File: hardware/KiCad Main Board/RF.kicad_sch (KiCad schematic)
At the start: 29 parts, among them U4 SI4468-A2A-IM, U6 CC1120RHBR, Y2 RTX-104EF3C-S-30.000-TR, Y3 END4263D-32M

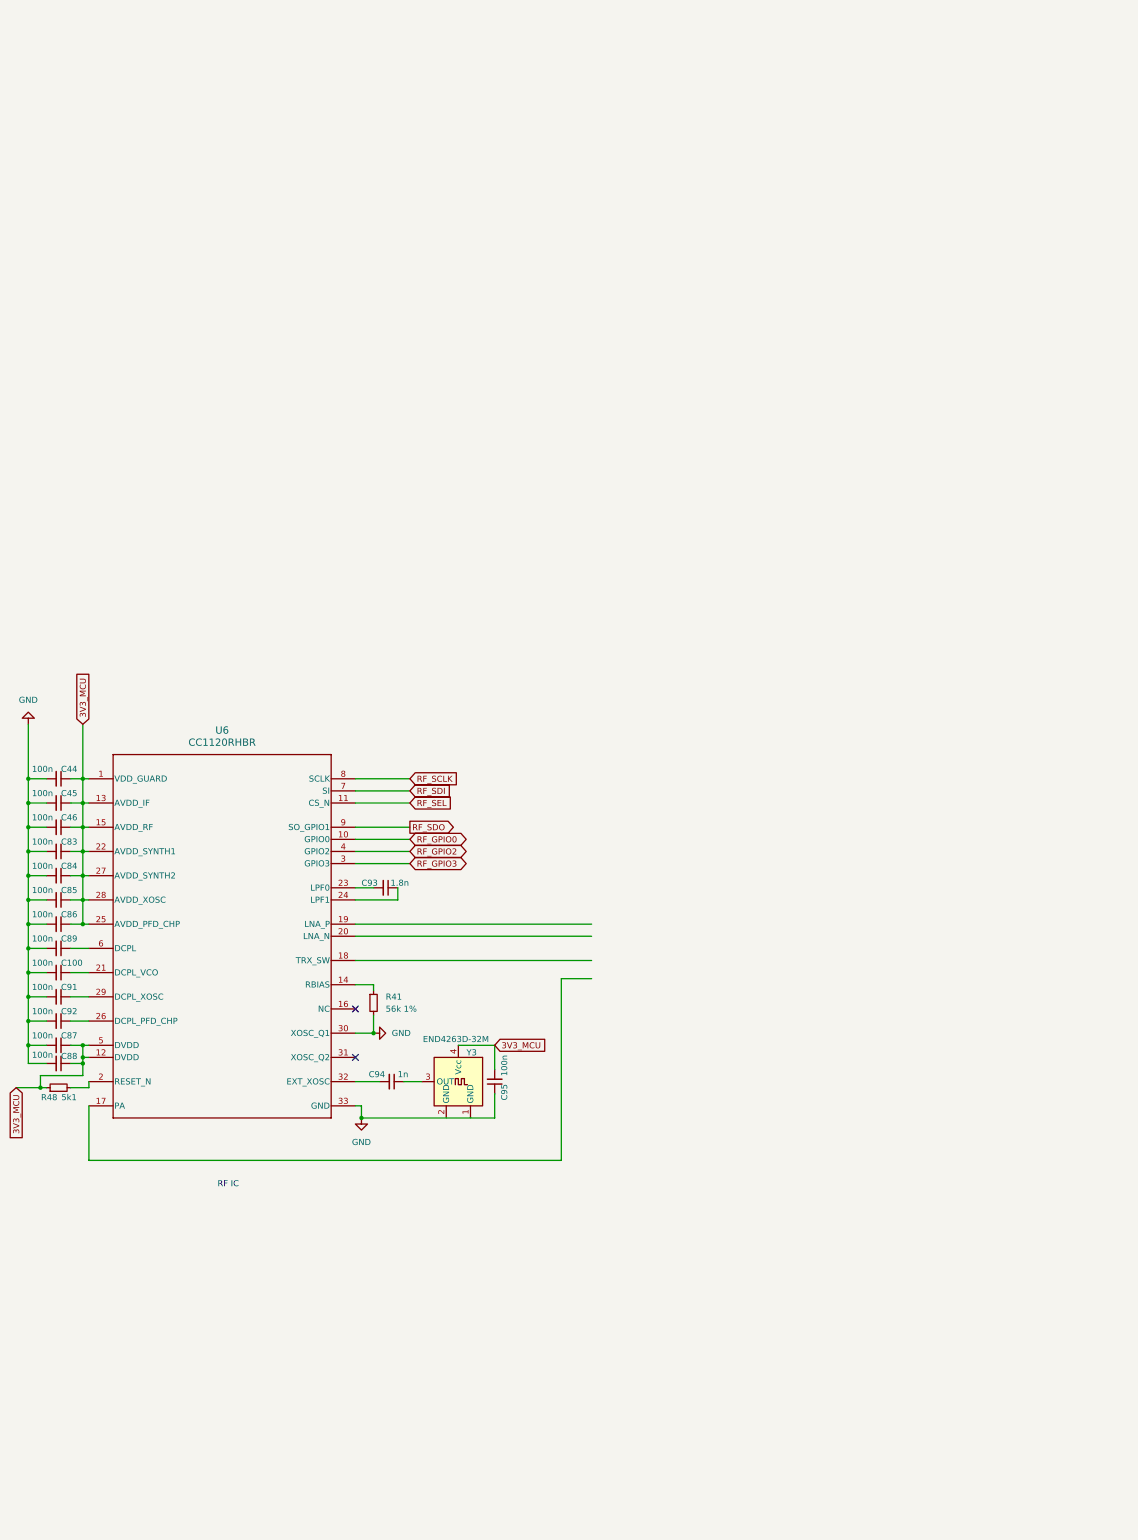
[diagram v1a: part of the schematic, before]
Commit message: added connector for RF daughter board
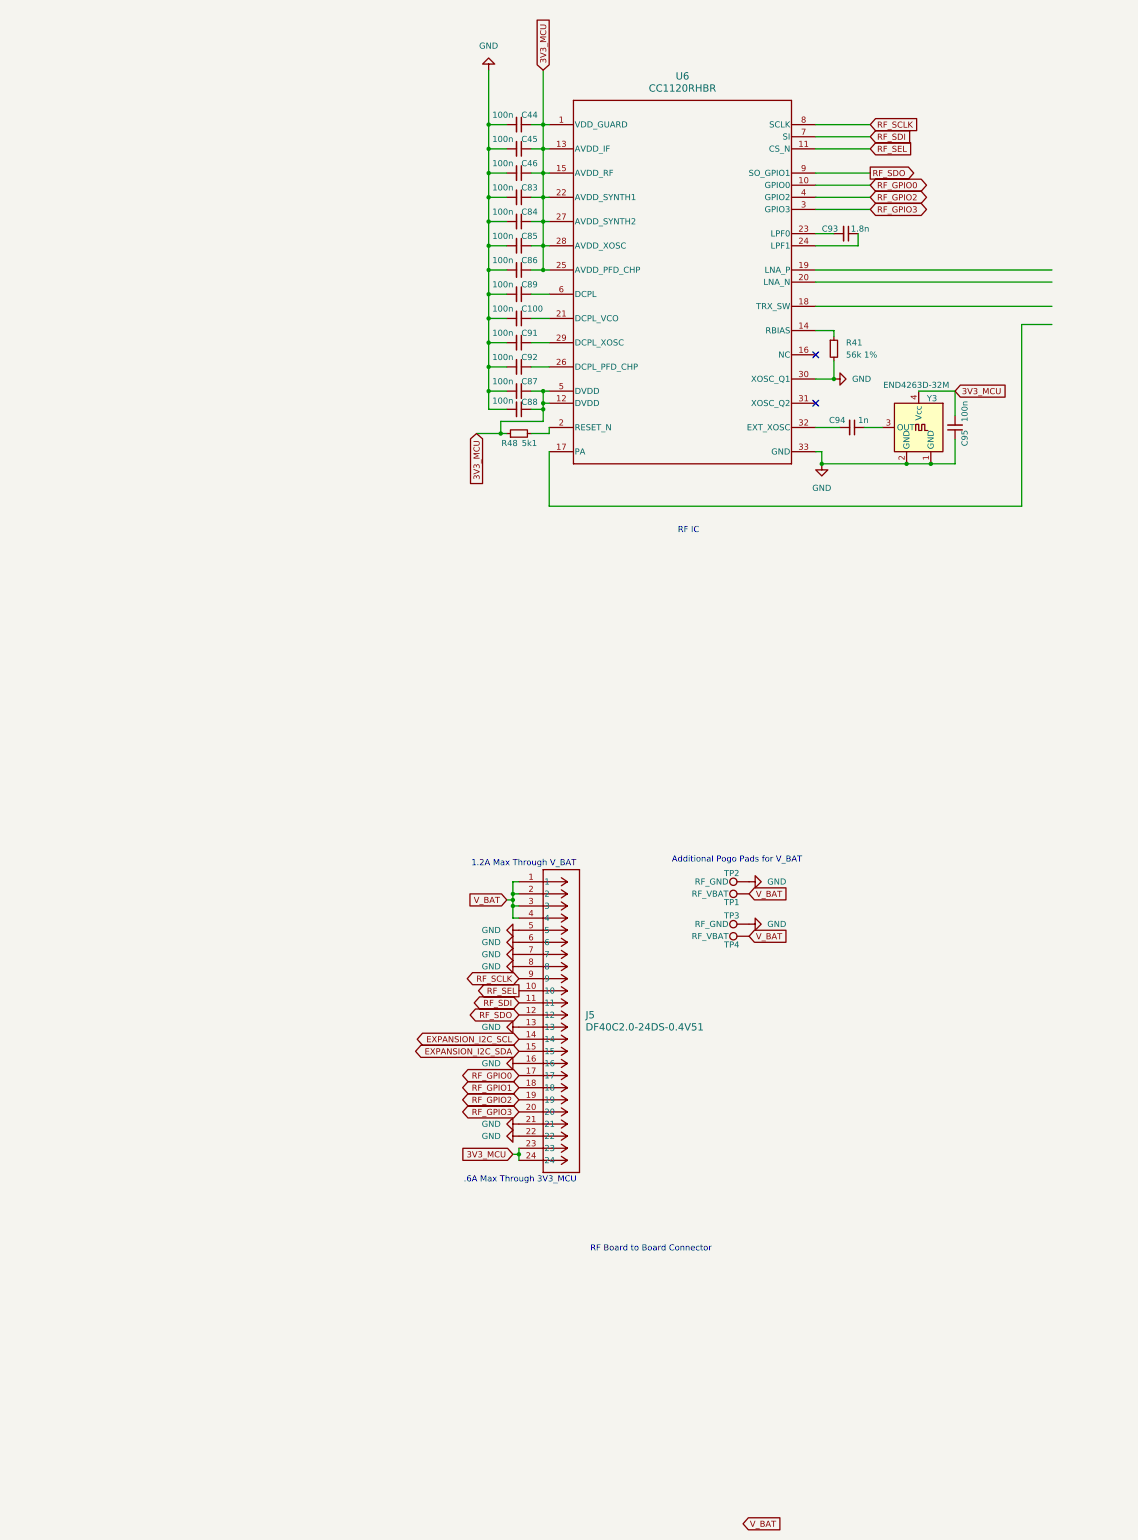
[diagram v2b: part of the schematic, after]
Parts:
- added J5: DF40C2.0-24DS-0.4V51, CONN24_DF40C-2-24DS_HIR, symbol 2025-04-19_21-20-12:DF40C2.0-24DS-0.4V51
- added TP1, TP4: RF_VBAT, TestPoint:TestPoint_Pad_D2.5mm, symbol Connector:TestPoint
- added TP2, TP3: RF_GND, TestPoint:TestPoint_Pad_D2.5mm, symbol Connector:TestPoint
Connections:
- net 3V3_MCU: now also J5.23, J5.24
- net GND: now also Y3.1 (GND), Y3.2 (GND), J5.13, J5.16, J5.21, J5.22, J5.5, J5.6, J5.7, J5.8, TP2.1, TP3.1
- net RF_GPIO0: now also J5.17
- net RF_GPIO1: now also J5.18
- net RF_GPIO2: now also J5.19
- net RF_GPIO3: now also J5.20
- net RF_SCLK: now also J5.9
- net RF_SDI: now also J5.11
- net RF_SDO: now also J5.12
- net RF_SEL: now also J5.10
- new net EXPANSION_I2C_SCL: J5.14
- new net EXPANSION_I2C_SDA: J5.15
- new net V_BAT: J5.1, J5.2, J5.3, J5.4, TP1.1, TP4.1
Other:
- note added: ".6A Max Through 3V3_MCU"
- note added: "1.2A Max Through V_BAT"
- note added: "Additional Pogo Pads for V_BAT"
- note added: "RF Board to Board Connector"
- moved on the sheet: C100, C44, C45, C46, C83, C84, C85, C86, C87, C88, C89, C91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

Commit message: working on PCB
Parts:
- removed C20: 4.7u, symbol Device:C_Small
- removed C21, C24: 100n, symbol Device:C_Small
- removed C22, C25: 100p, symbol Device:C_Small
- removed C23: 15p, symbol Device:C_Small
- removed R11: 10k, symbol Device:R_Small
- removed U4: SI4468-A2A-IM, QFN20_4X4_SIL, symbol 2025-03-28_00-57-05:SI4468-A2A-IM
- removed Y2: RTX-104EF3C-S-30.000-TR, Crystal:Crystal_SMD_3225-4Pin_3.2x2.5mm, symbol Device:Crystal_GND23
- added U14: AT24CS01-SSHM, Package_SO:SOIC-8_3.9x4.9mm_P1.27mm, symbol Memory_EEPROM:AT24CS01-SSHM
- J5: footprint CONN24_DF40C-2-24DS_HIR -> DF40C-24DS:CONN24_DF40C-2-24DS_HIR
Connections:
- net EXPANSION_I2C_SDA: now also J5.13; no longer J5.15
- net GND: now also J5.10, J5.11, J5.12, J5.9; no longer J5.13, J5.16, J5.21, J5.22, J5.5
- net RF_GPIO0: now also J5.19; no longer J5.17
- net RF_GPIO1: now also J5.20; no longer J5.18
- net RF_GPIO2: now also J5.21; no longer J5.19
- net RF_GPIO3: now also J5.22; no longer J5.20
- net RF_SCLK: now also J5.15; no longer J5.9
- net RF_SDI: now also J5.16; no longer J5.11
- net RF_SDO: now also J5.17; no longer J5.12
- net RF_SEL: now also J5.18; no longer J5.10
- net V_BAT: now also J5.5

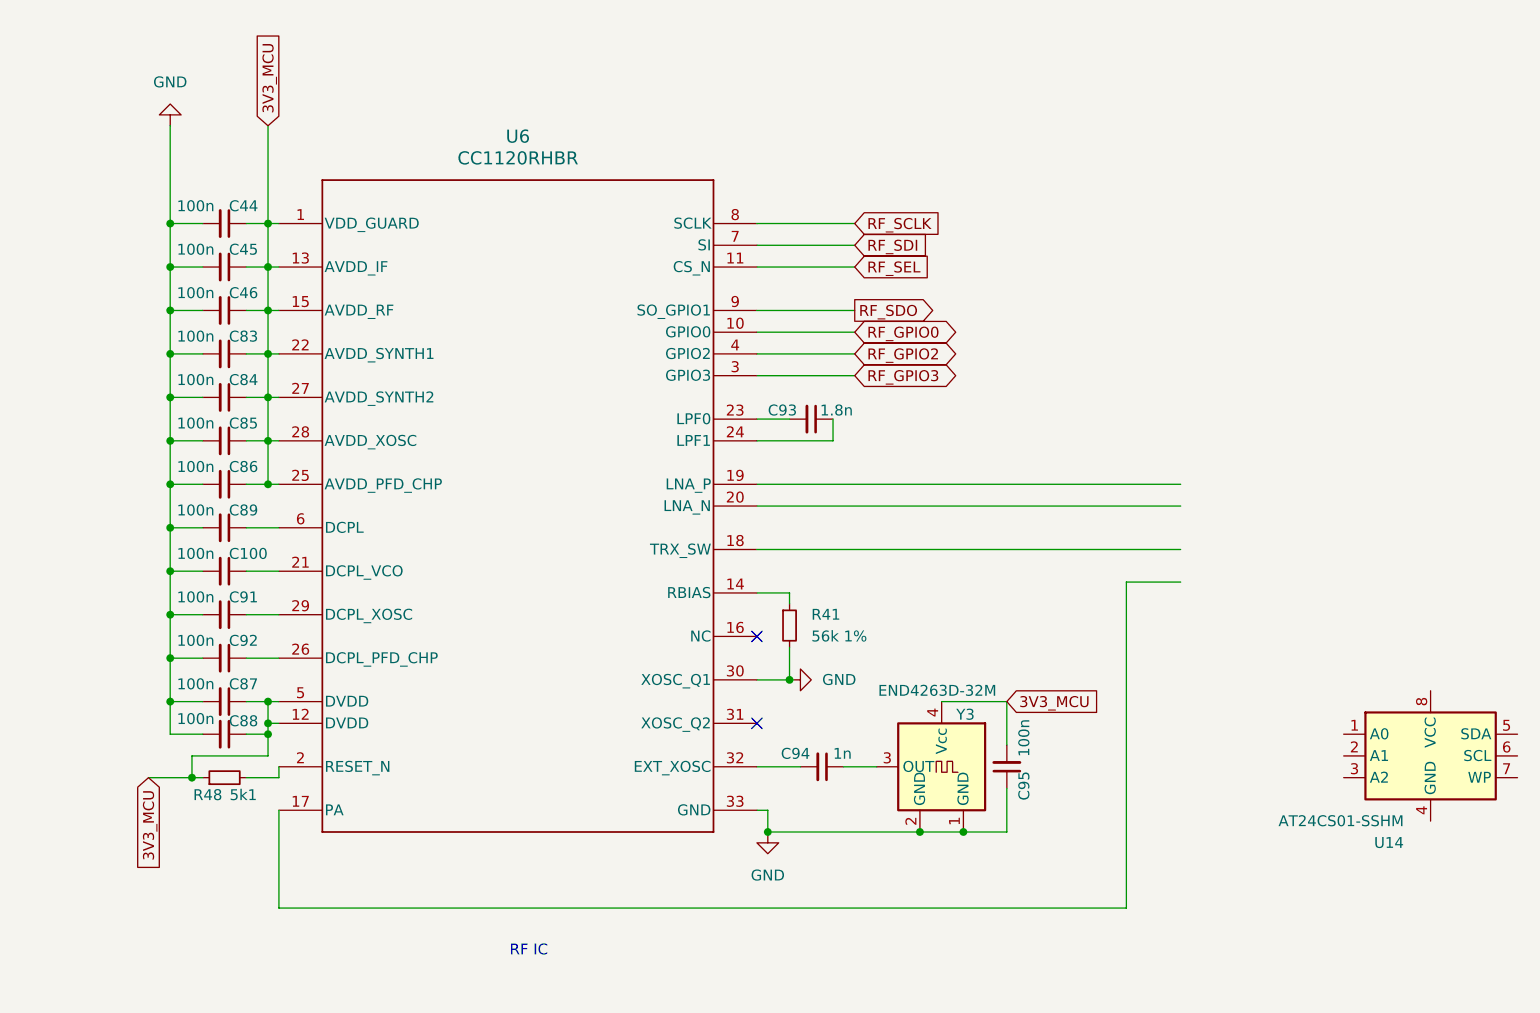
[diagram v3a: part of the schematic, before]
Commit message: all GPIO nets connected on schematic
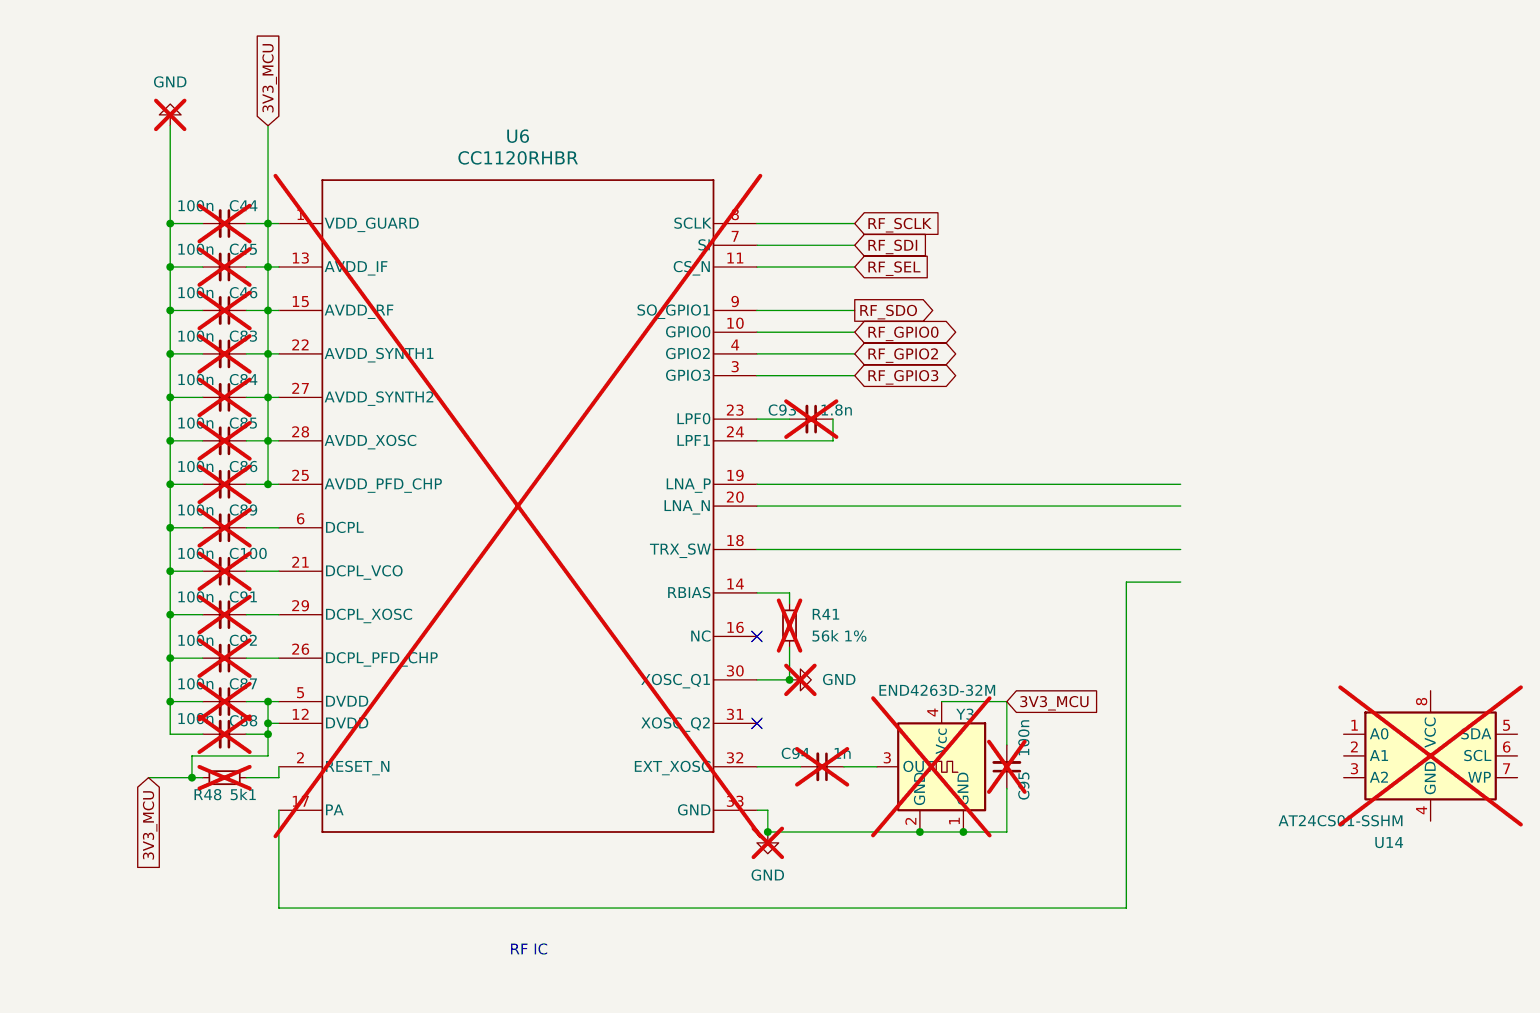
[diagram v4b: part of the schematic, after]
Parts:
- C100, C44, C45, C46, C83, C84, C85, C86, C87, C88, C89, C91, C92, C93, C94, C95, R41, R48, U14, U6, Y3: now not fitted; now left out of the parts list
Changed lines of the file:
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@@
 		(at 121.92 -74.93 270)
 		(unit 1)
-		(exclude_from_sim no)
-		(in_bom yes)
-		(on_board no)
-		(dnp no)
+		(exclude_from_sim yes)
+		(in_bom no)
+		(on_board no)
+		(dnp yes)
 		(property "Reference" "C84"
 			(at 122.428 -76.962 90)
@@
 		(at 121.92 -90.17 270)
 		(unit 1)
-		(exclude_from_sim no)
-		(in_bom yes)
-		(on_board no)
-		(dnp no)
+		(exclude_from_sim yes)
+		(in_bom no)
+		(on_board no)
+		(dnp yes)
 		(property "Reference" "C45"
 			(at 122.428 -92.202 90)
@@
 		(at 121.92 -59.69 270)
 		(unit 1)
-		(exclude_from_sim no)
-		(in_bom yes)
-		(on_board no)
-		(dnp no)
+		(exclude_from_sim yes)
+		(in_bom no)
+		(on_board no)
+		(dnp yes)
 		(property "Reference" "C89"
 			(at 122.428 -61.722 90)
@@
 		(at 121.92 -35.56 270)
 		(unit 1)
-		(exclude_from_sim no)
-		(in_bom yes)
-		(on_board no)
-		(dnp no)
+		(exclude_from_sim yes)
+		(in_bom no)
+		(on_board no)
+		(dnp yes)
 		(property "Reference" "C88"
 			(at 122.428 -37.084 90)
@@
 		(at 191.77 -31.75 270)
 		(unit 1)
-		(exclude_from_sim no)
-		(in_bom yes)
-		(on_board no)
-		(dnp no)
+		(exclude_from_sim yes)
+		(in_bom no)
+		(on_board no)
+		(dnp yes)
 		(property "Reference" "C94"
 			(at 186.944 -33.274 90)
@@
 		(at 121.92 -69.85 270)
 		(unit 1)
-		(exclude_from_sim no)
-		(in_bom yes)
-		(on_board no)
-		(dnp no)
+		(exclude_from_sim yes)
+		(in_bom no)
+		(on_board no)
+		(dnp yes)
 		(property "Reference" "C85"
 			(at 122.428 -71.882 90)
@@
 		(mirror y)
 		(unit 1)
-		(exclude_from_sim no)
-		(in_bom yes)
-		(on_board no)
-		(dnp no)
+		(exclude_from_sim yes)
+		(in_bom no)
+		(on_board no)
+		(dnp yes)
 		(property "Reference" "Y3"
 			(at 208.534 -37.846 0)
@@
 		(at 262.89 -33.02 0)
 		(unit 1)
-		(exclude_from_sim no)
-		(in_bom yes)
-		(on_board no)
-		(dnp no)
+		(exclude_from_sim yes)
+		(in_bom no)
+		(on_board no)
+		(dnp yes)
 		(property "Reference" "U14"
 			(at 259.7719 -22.86 0)
@@
 		(at 121.92 -39.37 270)
 		(unit 1)
-		(exclude_from_sim no)
-		(in_bom yes)
-		(on_board no)
-		(dnp no)
+		(exclude_from_sim yes)
+		(in_bom no)
+		(on_board no)
+		(dnp yes)
 		(property "Reference" "C87"
 			(at 122.428 -41.402 90)
@@
 		(at 121.92 -44.45 270)
 		(unit 1)
-		(exclude_from_sim no)
-		(in_bom yes)
-		(on_board no)
-		(dnp no)
+		(exclude_from_sim yes)
+		(in_bom no)
+		(on_board no)
+		(dnp yes)
 		(property "Reference" "C92"
 			(at 122.428 -46.482 90)
@@
 		(at 121.92 -85.09 270)
 		(unit 1)
-		(exclude_from_sim no)
-		(in_bom yes)
-		(on_board no)
-		(dnp no)
+		(exclude_from_sim yes)
+		(in_bom no)
+		(on_board no)
+		(dnp yes)
 		(property "Reference" "C46"
 			(at 122.428 -87.122 90)
@@
 		(at 121.92 -49.53 270)
 		(unit 1)
-		(exclude_from_sim no)
-		(in_bom yes)
-		(on_board no)
-		(dnp no)
+		(exclude_from_sim yes)
+		(in_bom no)
+		(on_board no)
+		(dnp yes)
 		(property "Reference" "C91"
 			(at 122.428 -51.562 90)
@@
 		(at 156.21 -62.23 0)
 		(unit 1)
-		(exclude_from_sim no)
-		(in_bom yes)
-		(on_board no)
-		(dnp no)
+		(exclude_from_sim yes)
+		(in_bom no)
+		(on_board no)
+		(dnp yes)
 		(fields_autoplaced yes)
 		(property "Reference" "U6"
@@
 		(at 115.57 -106.68 180)
 		(unit 1)
-		(exclude_from_sim no)
-		(in_bom yes)
-		(on_board no)
-		(dnp no)
+		(exclude_from_sim yes)
+		(in_bom no)
+		(on_board no)
+		(dnp yes)
 		(fields_autoplaced yes)
 		(property "Reference" "#PWR029"
@@
 		(at 121.92 -30.48 90)
 		(unit 1)
-		(exclude_from_sim no)
-		(in_bom yes)
-		(on_board no)
-		(dnp no)
+		(exclude_from_sim yes)
+		(in_bom no)
+		(on_board no)
+		(dnp yes)
 		(property "Reference" "R48"
 			(at 121.666 -28.448 90)
@@
 		(at 121.92 -80.01 270)
 		(unit 1)
-		(exclude_from_sim no)
-		(in_bom yes)
-		(on_board no)
-		(dnp no)
+		(exclude_from_sim yes)
+		(in_bom no)
+		(on_board no)
+		(dnp yes)
 		(property "Reference" "C83"
 			(at 122.428 -82.042 90)
@@
 		(at 213.36 -31.75 180)
 		(unit 1)
-		(exclude_from_sim no)
-		(in_bom yes)
-		(on_board no)
-		(dnp no)
+		(exclude_from_sim yes)
+		(in_bom no)
+		(on_board no)
+		(dnp yes)
 		(property "Reference" "C95"
 			(at 215.392 -31.242 90)
@@
 		(at 187.96 -41.91 90)
 		(unit 1)
-		(exclude_from_sim no)
-		(in_bom yes)
-		(on_board no)
-		(dnp no)
+		(exclude_from_sim yes)
+		(in_bom no)
+		(on_board no)
+		(dnp yes)
 		(fields_autoplaced yes)
 		(property "Reference" "#PWR046"
@@
 		(at 121.92 -64.77 270)
 		(unit 1)
-		(exclude_from_sim no)
-		(in_bom yes)
-		(on_board no)
-		(dnp no)
+		(exclude_from_sim yes)
+		(in_bom no)
+		(on_board no)
+		(dnp yes)
 		(property "Reference" "C86"
 			(at 122.428 -66.802 90)
@@
 		(at 190.5 -72.39 270)
 		(unit 1)
-		(exclude_from_sim no)
-		(in_bom yes)
-		(on_board no)
-		(dnp no)
+		(exclude_from_sim yes)
+		(in_bom no)
+		(on_board no)
+		(dnp yes)
 		(property "Reference" "C93"
 			(at 185.42 -73.406 90)
@@
 		(at 187.96 -48.26 0)
 		(unit 1)
-		(exclude_from_sim no)
-		(in_bom yes)
-		(on_board no)
-		(dnp no)
+		(exclude_from_sim yes)
+		(in_bom no)
+		(on_board no)
+		(dnp yes)
 		(fields_autoplaced yes)
 		(property "Reference" "R41"
@@
 		(at 121.92 -54.61 270)
 		(unit 1)
-		(exclude_from_sim no)
-		(in_bom yes)
-		(on_board no)
-		(dnp no)
+		(exclude_from_sim yes)
+		(in_bom no)
+		(on_board no)
+		(dnp yes)
 		(property "Reference" "C100"
 			(at 122.428 -56.642 90)
@@
 		(at 121.92 -95.25 270)
 		(unit 1)
-		(exclude_from_sim no)
-		(in_bom yes)
-		(on_board no)
-		(dnp no)
+		(exclude_from_sim yes)
+		(in_bom no)
+		(on_board no)
+		(dnp yes)
 		(property "Reference" "C44"
 			(at 122.428 -97.282 90)
@@
 		(at 185.42 -24.13 0)
 		(unit 1)
-		(exclude_from_sim no)
-		(in_bom yes)
-		(on_board no)
-		(dnp no)
+		(exclude_from_sim yes)
+		(in_bom no)
+		(on_board no)
+		(dnp yes)
 		(fields_autoplaced yes)
 		(property "Reference" "#PWR031"

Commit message: mostly designed PCB
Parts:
- added H5, H6, H7, H8: MountingHole, MountingHole:MountingHole_2.2mm_M2_ISO14580, symbol Mechanical:MountingHole
